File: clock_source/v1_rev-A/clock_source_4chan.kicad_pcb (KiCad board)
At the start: 2 copper layers, 25.4 x 31.8 mm, 44 parts, among them J0 Y0, J1 Y1, J2 Y2, J3 Y3, U1 5PB1104PGxx, U2 SPX3819M5-L-3-3, U3 SN74LVC2G14DBV, Y1 TCXO_B31

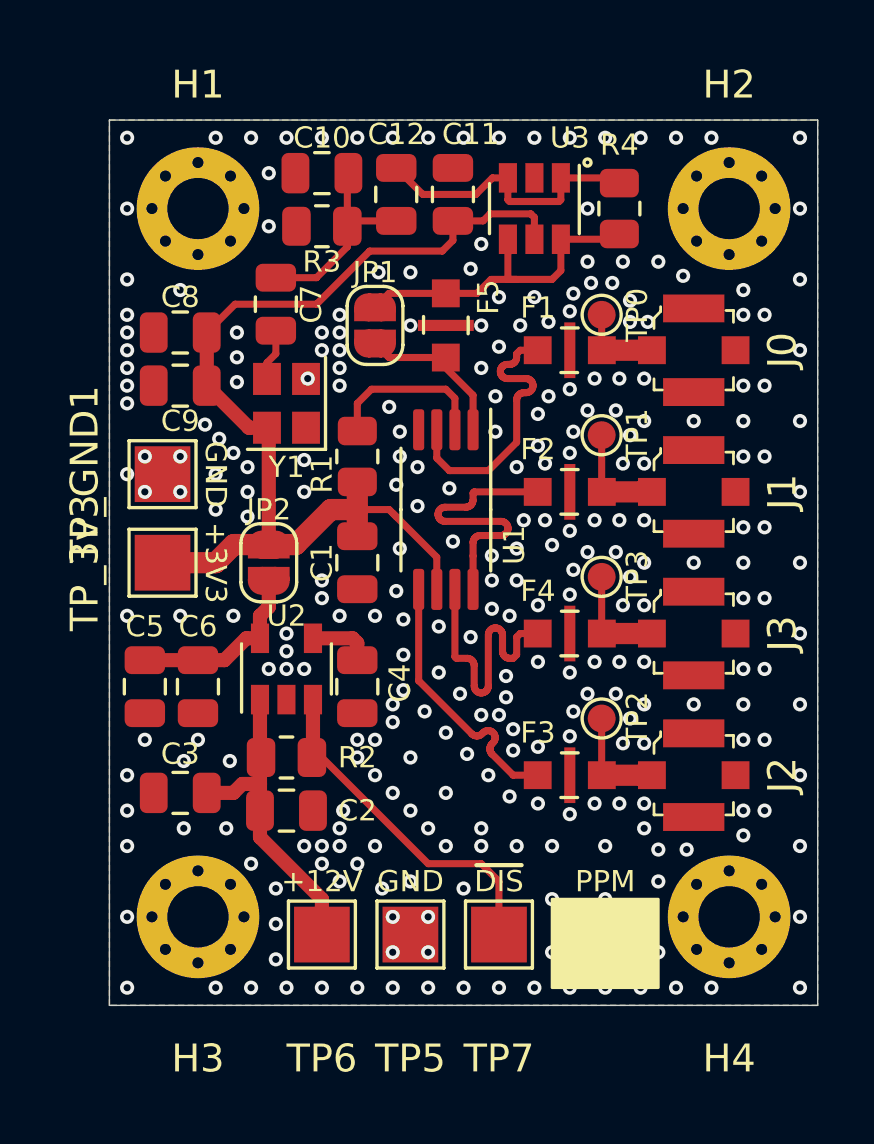
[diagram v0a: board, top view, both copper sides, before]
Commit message: adding new KiCAD 6 files.
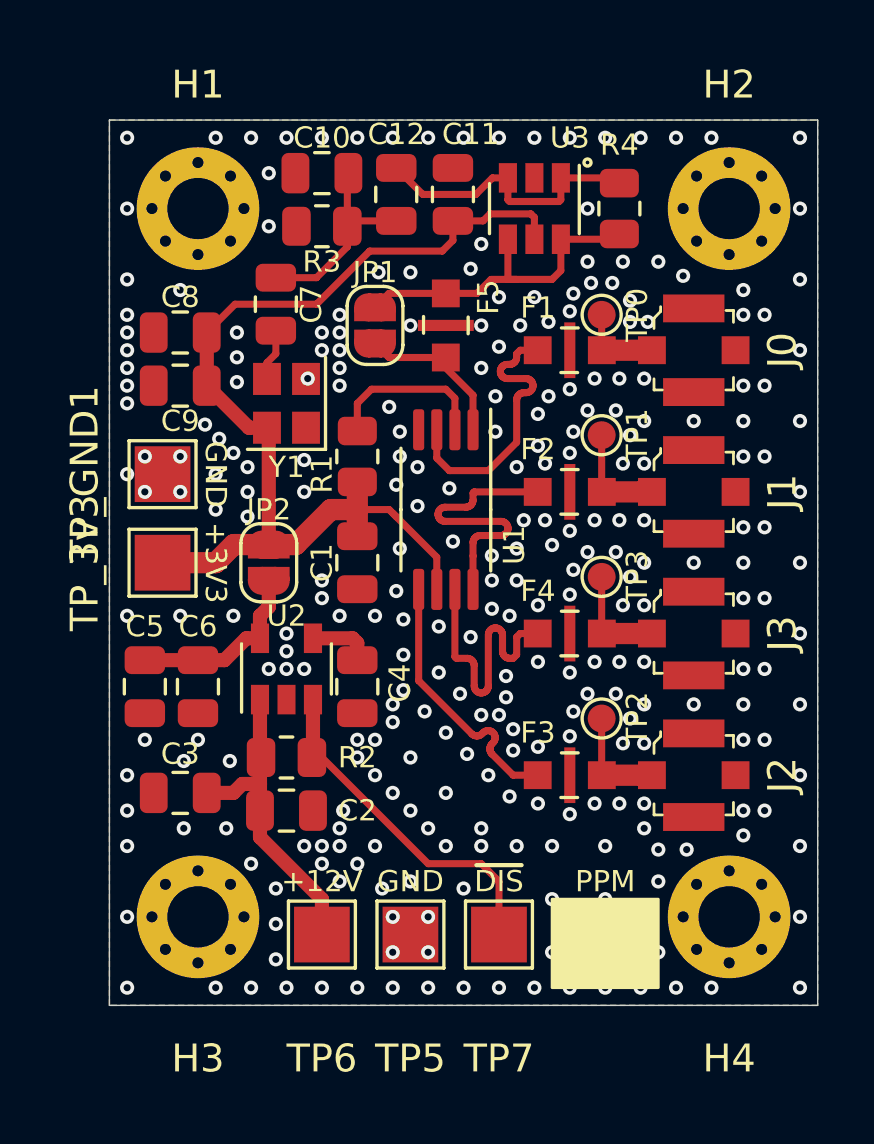
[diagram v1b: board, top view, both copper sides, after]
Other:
- net class Default removed
- board text added: "0.75""
- board text added: "1""
- board text added: "1.25""
- board text added: "~{DIS}"
- board text removed: "0.75"
- board text removed: "1"
- board text removed: "~DIS"
